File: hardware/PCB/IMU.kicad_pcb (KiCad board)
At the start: 2 copper layers, 32.5 x 19.5 mm, 31 parts, among them J1 USB_A, SW1 SW_Push, U1 RP2040, U2 ICM-45686, U6 NCP1117-3.3_SOT223, U7 W25Q128JVS, Y1 12 MHz

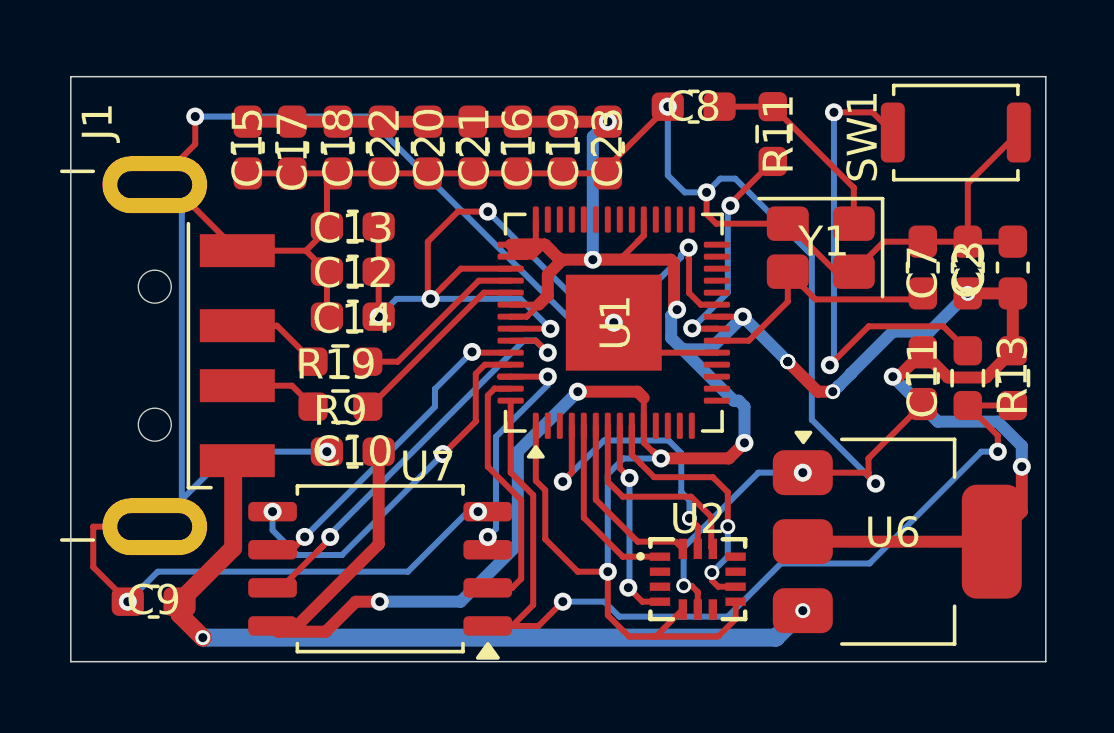
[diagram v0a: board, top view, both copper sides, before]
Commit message: Reworked PCB
Moved Decoupeling Capacitors physically closer to buck converter and RP2040.
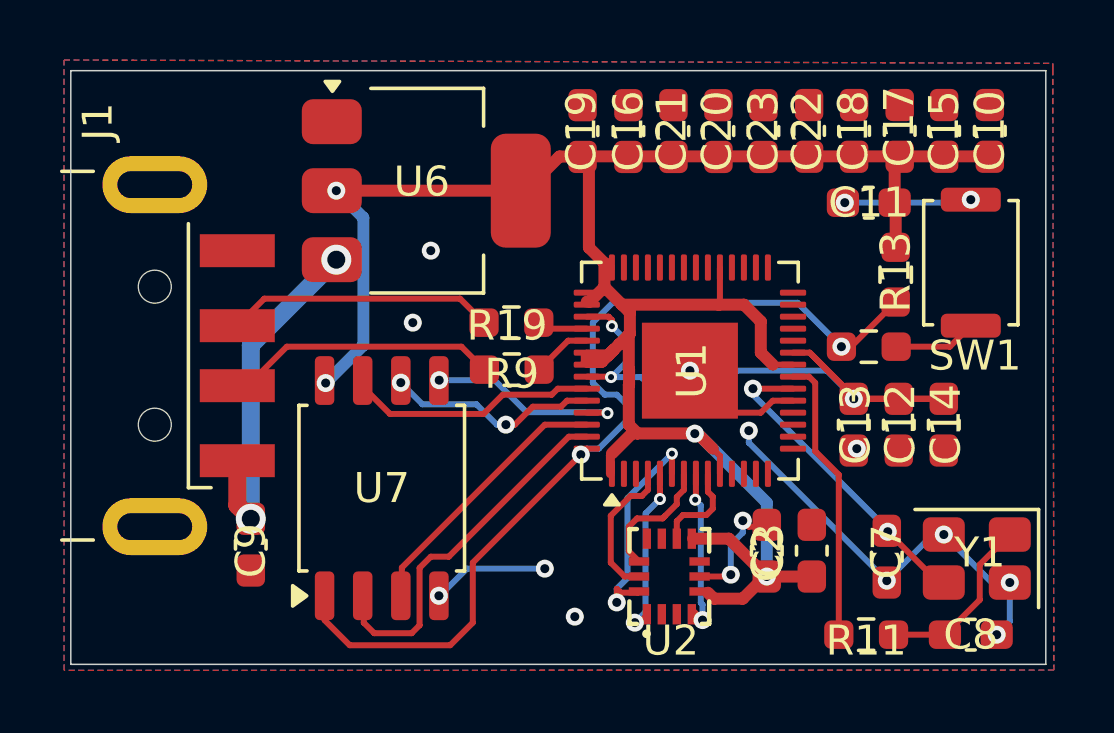
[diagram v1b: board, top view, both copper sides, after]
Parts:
- moved C10 23.8 mm to (125.2, 69.8), turned to 90 degrees
- moved C15 23.2 mm to (123.7, 69.8), turned to 90 degrees
- moved C17 20.3 mm to (122.2, 69.8), turned to 90 degrees
- moved C14 20.0 mm to (123.7, 79.6), turned to -90 degrees
- moved C8 19.9 mm to (124.6, 86.6), turned to 180 degrees
- moved U6 19.6 mm to (106.5, 71.8)
- moved C12 18.9 mm to (122.2, 79.6), turned to -90 degrees
- moved C13 18.0 mm to (120.7, 79.6), turned to -90 degrees
- moved C18 17.2 mm to (120.7, 69.8), turned to 90 degrees
- moved R11 17.0 mm to (121.1, 86.6), turned to 180 degrees
- moved C22 14.2 mm to (119.2, 69.8), turned to 90 degrees
- moved Y1 11.6 mm to (124.8, 84.1)
- moved C2 11.6 mm to (117.8, 83.8)
- moved C3 11.6 mm to (119.3, 83.8)
- moved C7 9.71 mm to (121.8, 84.0), turned to 90 degrees
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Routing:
- net GND: track 136.2 -> 30.7 mm, vias 10 -> 16
- net +3.3V: track 148.9 -> 74.3 mm, vias 15 -> 4
- net VBUS: track 28.1 -> 12.0 mm
- net Net-(R12-Pad1): track 16.2 -> 2.78 mm, vias 2 -> 0
- net USB_DP: track 2.81 -> 9.79 mm
- net /ICM_INT2: track 9.68 -> 3.18 mm, vias 2 -> 0
- net +1V1: track 30.3 -> 24.0 mm, vias 5 -> 3
- net QSPI_SD3: track 14.5 -> 8.40 mm, vias 2 -> 0
- net USB_DM: track 3.02 -> 8.93 mm
- net QSPI_SD0: track 12.5 -> 6.78 mm
- net /ICM_SCK: track 10.1 -> 4.83 mm, vias 2 -> 0
- net Net-(U1-USB_DP): track 6.34 -> 1.99 mm
- net Net-(U1-USB_DM): track 5.88 -> 1.68 mm
- net QSPI_SCLK: track 11.0 -> 7.18 mm
- net QSPI_SD1: track 8.67 -> 12.2 mm
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- added copper zone on B.Cu, net GND
- added copper zone on F.Cu, net GND
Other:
- board size 32.5 x 19.5 mm -> 32.5 x 19.8 mm
